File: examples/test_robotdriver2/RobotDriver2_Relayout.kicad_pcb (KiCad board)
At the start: 2 copper layers, 110 x 58 mm, 80 parts, among them SW1 C318884, U1 C7972, U2 C500769, U3 C701342, U4 C967633, U5 C86832, U6 C50506, U7 C50506

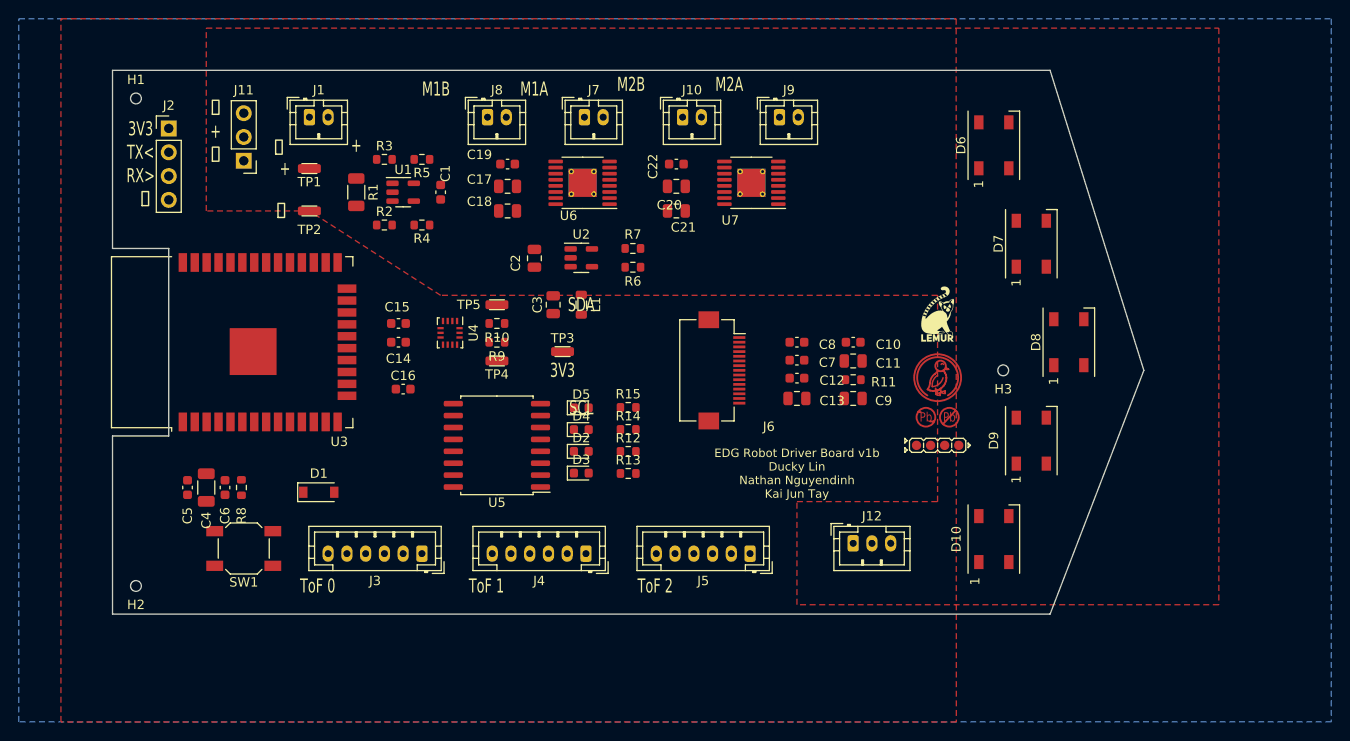
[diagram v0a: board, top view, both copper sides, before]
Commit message: Basic routing done on PCB
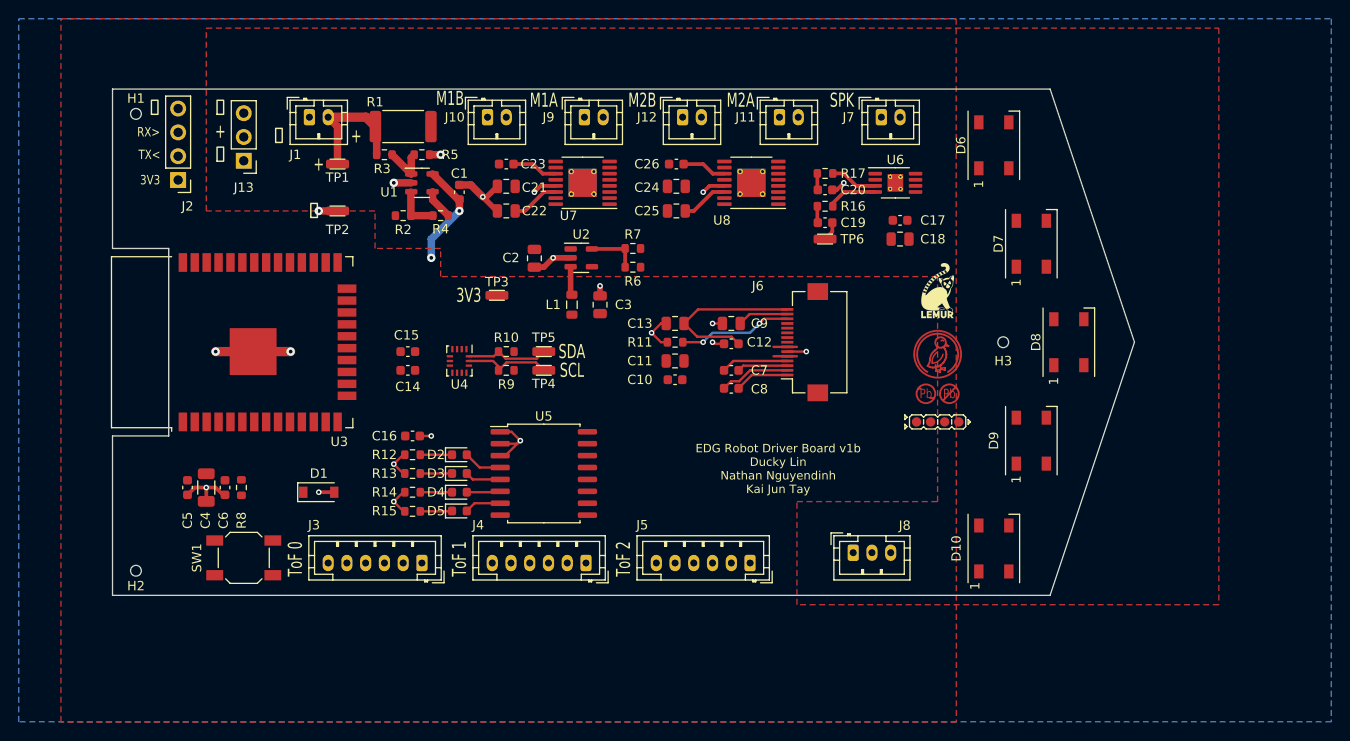
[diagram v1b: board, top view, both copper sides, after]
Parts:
- added C17: CC0603KRX7R9BB104 (YAGEO) - 50V 100nF X7R ±10% 0603 Multila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, Capacitor_SMD:C_0603_1608Metric, F.Cu at (179.0, 69.0)
- added C18: CL21A475KAQNNNE (Samsung Electro-Mechanics) - 25V 4.7uF X5R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, Capacitor_SMD:C_0805_2012Metric, F.Cu at (179.0, 71.0)
- added C19: CL10A105KB8NNNC (Samsung Electro-Mechanics) - 50V 1uF X5R ±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, Capacitor_SMD:C_0603_1608Metric, F.Cu at (171.0, 69.2)
- added C20: CL10A105KB8NNNC (Samsung Electro-Mechanics) - 50V 1uF X5R ±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, Capacitor_SMD:C_0603_1608Metric, F.Cu at (171.0, 65.8)
- added J7: B2B-PH-K (JST), Connector_JST:JST_PH_B2B-PH-K_1x02_P2.00mm_Vertical, F.Cu at (177.0, 58.0)
- added R16: 0603WAF3002T5E (UNI-ROYAL(Uniroyal Elec)) - ±1% 1/10W Thick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, Resistor_SMD:R_0603_1608Metric, F.Cu at (171.0, 67.5)
- added R17: 0603WAF3002T5E (UNI-ROYAL(Uniroyal Elec)) - ±1% 1/10W Thick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, Resistor_SMD:R_0603_1608Metric, F.Cu at (171.0, 64.0)
- added TP6: RCU-0C (TE Connectivity) - spk_chain_0, edg:TestPoint_TE_RCU_0603, F.Cu at (171.0, 71.0)
- added U6: TPA2005D1 (Texas Instruments), Package_SO:MSOP-8-1EP_3x3mm_P0.65mm_EP1.68x1.88mm_ThermalVias, F.Cu at (178.5, 65.0)
- C1, C10, C12, C14, C15, C16, C5, C7, C8: value C14663 -> CC0603KRX7R9BB104 (YAGEO) - 50V 100nF X7R ±10% 0603 Multilayer Ceramic Capacitors MLCC - SMD/SMT ROHS
- C11, C2, C3, C9: value C1779 -> CL21A475KAQNNNE (Samsung Electro-Mechanics) - 25V 4.7uF X5R ±10% 0805 Multilayer Ceramic Capacitors MLCC - SMD/SMT ROHS
- C13: value C15850 -> CL21A106KAYNNNE (Samsung Electro-Mechanics) - X5R 25V ±10% 10uF 0805 Multilayer Ceramic Capacitors MLCC - SMD/SMT ROHS
- C21: renamed from C17; value C15850 -> CL21A106KAYNNNE (Samsung Electro-Mechanics) - X5R 25V ±10% 10uF 0805 Multilayer Ceramic Capacitors MLCC - SMD/SMT ROHS
- C22: renamed from C18; value C1779 -> CL21A475KAQNNNE (Samsung Electro-Mechanics) - 25V 4.7uF X5R ±10% 0805 Multilayer Ceramic Capacitors MLCC - SMD/SMT ROHS
- C23: renamed from C19; value C57112 -> 0603B103K500NT (FH(Guangdong Fenghua Advanced Tech)) - 50V 10nF X7R ±10% 0603 Multilayer Ceramic Capacitors MLCC - SMD/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
- C24: renamed from C20; value C15850 -> CL21A106KAYNNNE (Samsung Electro-Mechanics) - X5R 25V ±10% 10uF 0805 Multilayer Ceramic Capacitors MLCC - SMD/SMT ROHS
- C25: renamed from C21; value C1779 -> CL21A475KAQNNNE (Samsung Electro-Mechanics) - 25V 4.7uF X5R ±10% 0805 Multilayer Ceramic Capacitors MLCC - SMD/SMT ROHS
- C26: renamed from C22; value C57112 -> 0603B103K500NT (FH(Guangdong Fenghua Advanced Tech)) - 50V 10nF X7R ±10% 0603 Multilayer Ceramic Capacitors MLCC - SMD/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
- C4: value C5672 -> CL31A226KPHNNNE (Samsung Electro-Mechanics) - 10V 22uF X5R ±10% 1206 Multilayer Ceramic Capacitors MLCC - SMD/SMT ROHS
- C6: value C15849 -> CL10A105KB8NNNC (Samsung Electro-Mechanics) - 50V 1uF X5R ±10% 0603 Multilayer Ceramic Capacitors MLCC - SMD/SMT ROHS
- D1: value C499796 -> BZT52C3V6 (SMC(Sangdest Microelectronicstronic (Nanjing))) - 5μA@1V 90Ω Single 3.6V~3.8V 350mW 3.4V SOD-123 Zener Diode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
- D10, D6, D7, D8, D9: value C2920042 -> WS2812B (Worldsemi)
- D2, D3, D4, D5: value C2286 -> KT-0603R (Hubei KENTO Elec) - Red 615~630nm 1.9~2.2V 0603 Light Emitting Diodes (LED) RoHS
- J1: value (none) -> B2B-PH-K (JST)
- J10: renamed from J8; value (none) -> B2B-PH-K (JST)
- J11: renamed from J9; value (none) -> B2B-PH-K (JST)
- J12: renamed from J10; value (none) -> B2B-PH-K (JST)
- J13: renamed from J11; value (none) -> PinHeader2.54 1x3 (Generic)
- J2: value (none) -> PinHeader2.54 1x4 (Generic)
- J3, J4, J5: value (none) -> B6B-PH-K (JST)
- J6: value (none) -> FH12-15S-0.5SH (Hirose)
- J8: renamed from J12; value (none) -> B3B-PH-K (JST)
- J9: renamed from J7; value (none) -> B2B-PH-K (JST)
- L1: value C98331 -> MPL2012S3R3MHT (Sunlord) - 900mA 3.3uH ±20% 190mΩ 0805 Inductors (SMD) ROHS
- R1: value C411236 -> RTT25R050FTE (RALEC) - ±1% 1W Thick Film Resistors 200V ±500ppm/℃ -55℃~+155℃ 0.05Ω 2512 Chip Resistor - Surface Mount R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; footprint Resistor_SMD:R_1206_3216Metric -> Resistor_SMD:R_2512_6332Metric
- R10, R9: value C23162 -> 0603WAF4701T5E (UNI-ROYAL(Uniroyal Elec)) - ±1% 1/10W Thick Film Resistors 75V ±100ppm/℃ -55℃~+155℃ 4.7kΩ 0603 Chip Res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
- R11: value C23203 -> 0603WAF5603T5E (UNI-ROYAL(Uniroyal Elec)) - ±1% 1/10W Thick Film Resistors 75V ±100ppm/℃ -55℃~+155℃ 560kΩ 0603 Chip Res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
- R12, R13, R14, R15: value C21190 -> 0603WAF1001T5E (UNI-ROYAL(Uniroyal Elec)) - ±1% 1/10W Thick Film Resistors 75V ±100ppm/℃ -55℃~+155℃ 1kΩ 0603 Chip Resis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
- R2, R3, R8: value C25804 -> 0603WAF1002T5E (UNI-ROYAL(Uniroyal Elec)) - ±1% 1/10W Thick Film Resistors 75V ±100ppm/℃ -55℃~+155℃ 10kΩ 0603 Chip Resi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
- R4, R5: value C25803 -> 0603WAF2003T5E (UNI-ROYAL(Uniroyal Elec)) - ±1% 1/10W Thick Film Resistors 75V ±100ppm/℃ -55℃~+155℃ 200kΩ 0603 Chip Res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
- R6: value C23231 -> 0603WAF6802T5E (UNI-ROYAL(Uniroyal Elec)) - ±1% 1/10W Thick Film Resistors 75V ±100ppm/℃ -55℃~+155℃ 68kΩ 0603 Chip Resi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
- R7: value C22809 -> 0603WAF1502T5E (UNI-ROYAL(Uniroyal Elec)) - ±1% 1/10W Thick Film Resistors 75V ±100ppm/℃ -55℃~+155℃ 15kΩ 0603 Chip Resi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
- SW1: value C318884 -> 5.1mm switch
- TP1: value (none) -> RCU-0C (TE Connectivity) - anon_link_0
- TP2: value (none) -> RCU-0C (TE Connectivity) - gnd
- TP3: value (none) -> RCU-0C (TE Connectivity) - v3v3
- TP4: value (none) -> RCU-0C (TE Connectivity) - i2c_chain_0.scl
- TP5: value (none) -> RCU-0C (TE Connectivity) - i2c_tp.anon_link_1
- U1: value C7972 -> LMV321 (Texas Instruments)
- U10: renamed from U9; value (none) -> Duck
- U11: renamed from U10; value (none) -> LeadFree
- U12: renamed from U11; value (none) -> IdDots4
- U2: value C500769 -> AP3418 (Diodes Incorporated)
- U3: value C701342 -> ESP32-WROOM-32 (Espressif Systems)
- U4: value C967633 -> LSM6DS3TR-C (STMicroelectronics)
- U5: value C86832 -> PCF8574AT (NXP)
- U7: renamed from U6; value C50506 -> DRV8833PWP (Texas Instruments)
- U8: renamed from U7; value C50506 -> DRV8833PWP (Texas Instruments)
- U9: renamed from U8; value (none) -> Lemur
- moved R15 25.5 mm to (127.0, 100.0), turned to 180 degrees
- moved R14 24.0 mm to (127.0, 98.0), turned to 180 degrees
- moved R12 23.0 mm to (127.0, 94.0), turned to 180 degrees
- moved R13 23.0 mm to (127.0, 96.0), turned to 180 degrees
- moved C10 19.4 mm to (155.0, 86.0), turned to 180 degrees
- moved R11 19.4 mm to (155.0, 82.0), turned to 180 degrees
- moved C11 19.0 mm to (155.0, 84.0), turned to 180 degrees
- moved D5 17.0 mm to (132.0, 100.0)
- moved C13 15.3 mm to (155.0, 80.0), turned to 180 degrees
- moved C9 15.3 mm to (161.0, 80.0), turned to 180 degrees
- moved D4 14.6 mm to (132.0, 98.0)
- moved D2 13.0 mm to (132.0, 94.0)
- moved D3 13.0 mm to (132.0, 96.0)
- moved J6 9.32 mm to (168.8, 82.0), turned to 90 degrees
- moved TP3 9.22 mm to (136.0, 77.0)
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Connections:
- net isense.amp.rf.b renamed isense.amp.amp.inn
- net isense.amp.rg.b renamed isense.amp.r2.b
- net lcd.c1_cap.neg renamed lcd.device.c1n
- net lcd.c1_cap.pos renamed lcd.device.c1p
- net lcd.c2_cap.neg renamed lcd.device.c2n
- net lcd.c2_cap.pos renamed lcd.device.c2p
- net lcd.vcc_cap1.pwr renamed lcd.vcc_cap2.pwr
- net led[0].package.k renamed led[0].res.a
- net mcu.ic.chip_pu renamed mcu.en_pull.io
- net mcu.ic.uart0.tx renamed mcu.uart0.uart.rx
- net mcu.prog.a renamed mcu.ic.io0
- net motor_driver2.ic.vcp renamed motor_driver2.vcp_cap.pos
- net motor_driver2.ic.vint renamed motor_driver2.vint_cap.pwr
- net reg_3v3.fb.output renamed reg_3v3.ic.fb
- net reg_3v3.ic.sw renamed reg_3v3.power_path.switch
- net ws2812bArray.led[0].dout renamed ws2812bArray.led[1].din
- net ws2812bArray.led[2].din renamed ws2812bArray.led[1].dout
- net ws2812bArray.led[3].din renamed ws2812bArray.led[2].dout
- D10 pad 2: ws2812bArray.dout -> led_pixel.pins.2
- J5 pad 6: tof.xshut.2 -> expander.io.tof_xshut_2
- J8 pad 2: mcu.gpio.ledConnector -> led_pixel.pins.2
- U3 pad 10: mcu.gpio.lcd_reset -> mcu.gpio.lcd_dc
- U3 pad 11: mcu.gpio.lcd_cs -> spk_chain_0
- U3 pad 12: i2c_chain_0.sda -> mcu.gpio.lcd_reset
- U3 pad 13: i2c_chain_0.scl -> mcu.gpio.lcd_cs
- U3 pad 14: (no net) -> i2c_chain_0.sda
- U3 pad 16: mcu.adc.isense -> i2c_chain_0.scl
- U3 pad 23: (no net) -> mcu.gpio.ledArray
- U3 pad 4: mcu.gpio.ledArray -> mcu.adc.isense
- U3 pad 5: mcu.gpio.ledConnector -> (no net)
- U3 pad 7: lcd.spi.mosi -> (no net)
- U3 pad 8: lcd.spi.sck -> lcd.spi.mosi
- U3 pad 9: mcu.gpio.lcd_dc -> lcd.spi.sck
- U5 pad 10: expander.io.tof_xshut_1 -> tof.xshut.0
- U5 pad 11: tof.xshut.0 -> expander.io.tof_xshut_1
- U5 pad 12: (no net) -> expander.io.tof_xshut_2
- U5 pad 4: expander.io.led1 -> expander.io.led0
- U5 pad 5: expander.io.led0 -> expander.io.led1
- U5 pad 9: tof.xshut.2 -> (no net)
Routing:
- net gnd: track 0.00 -> 63.3 mm, vias 0 -> 21
- net lcd.vcc_cap2.pwr: track 0.00 -> 18.4 mm
- net v3v3: track 0.00 -> 16.5 mm, vias 0 -> 2
- net batt.pins.2: track 0.00 -> 13.9 mm
- net lcd.device.iref: track 0.00 -> 12.2 mm, vias 0 -> 2
- net i2c_chain_0.scl: track 0.00 -> 9.34 mm
- net i2c_chain_0.sda: track 0.00 -> 8.82 mm
- net lcd.device.c2n: track 0.00 -> 7.54 mm
- net lcd.device.c1n: track 0.00 -> 7.19 mm
- net lcd.device.c2p: track 0.00 -> 5.79 mm
- net reg_3v3.ic.fb: track 0.00 -> 5.56 mm
- net lcd.vcomh_cap.pos: track 0.00 -> 5.46 mm
- net lcd.device.c1p: track 0.00 -> 5.41 mm
- net spk_drv.(adapter)inp_res.b.src: track 0.00 -> 5.35 mm
- net spk_drv.(adapter)inn_res.b.dst: track 0.00 -> 5.07 mm
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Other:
- board size 110 x 58 mm -> 109 x 54 mm
- board text added: "SPK"
